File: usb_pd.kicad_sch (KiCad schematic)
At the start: 34 parts, among them J1 USB-C_GCT_USB4105-GF-A, J2 JST_SH_1x4_SM04B-SRSS-TB-LF-SN, Q1 SQS401EN-T1_BE3, U1 STUSB4500_QFN, U5 TPD4E02B04DQA, U6 TPD4E02B04DQA

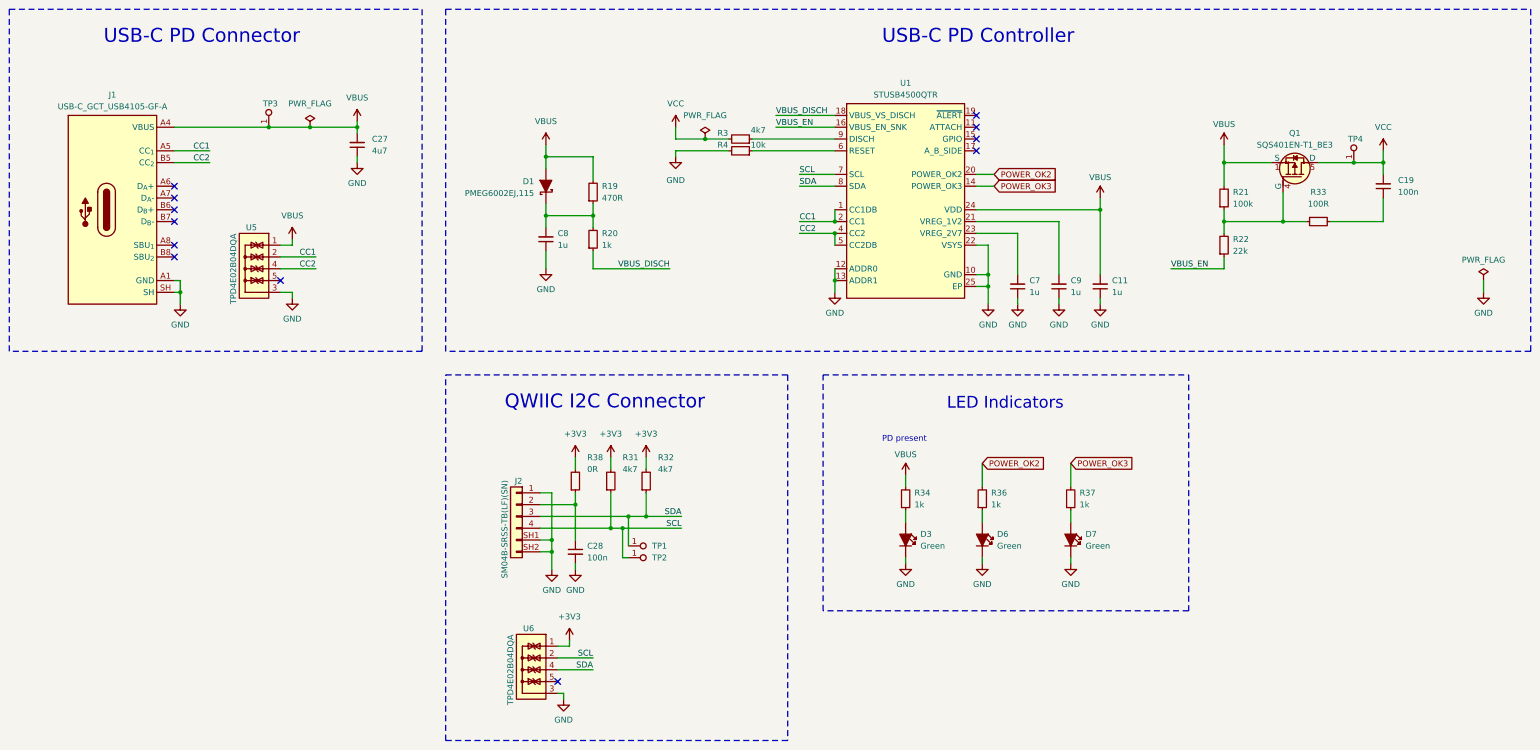
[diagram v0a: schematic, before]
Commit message: [#57006] Change capacitors to higher voltage ratings
Homogenize capacitors (to not use multiple versions of the same params)
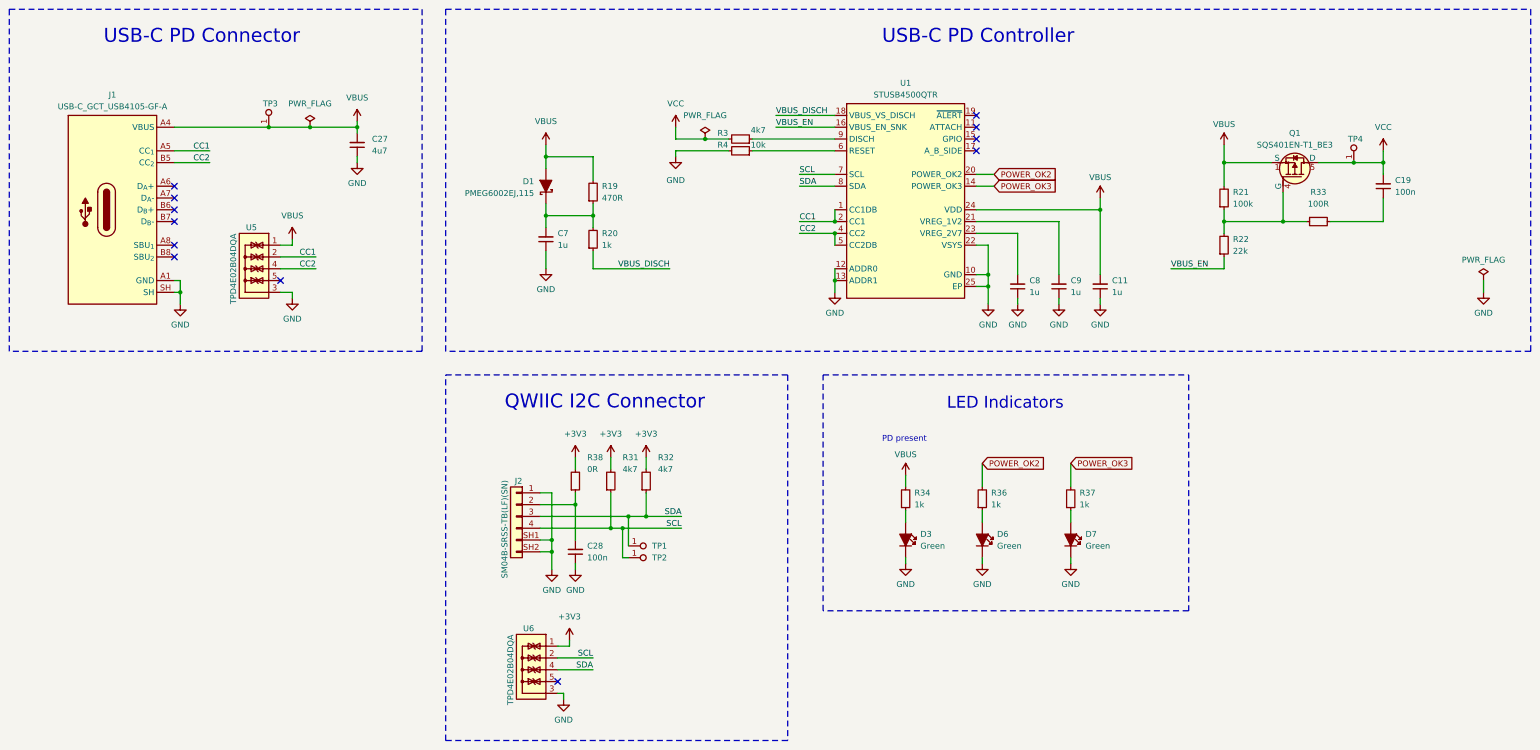
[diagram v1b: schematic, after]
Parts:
- removed C11, C7, C8, C9: C_1u_0402, antmicro-footprints:C_0402_1005Metric, symbol antmicroCapacitors0402:C_1u_0402
- removed C28: C_100n_16V_X7R_0402, antmicro-footprints:C_0402_1005Metric, symbol antmicroCapacitors0402:C_100n_16V_X7R_0402
- added C11, C7, C8, C9: C_1u_25V_0402, antmicro-footprints:C_0402_1005Metric, symbol antmicroCapacitors0402:C_1u_25V_0402
- added C28: C_100n_50V_X8L_0402, antmicro-footprints:C_0402_1005Metric, symbol antmicroCapacitors0402:C_100n_50V_X8L_0402
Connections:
- net GND: now also C11.1, C28.1, C7.1, C8.1, C9.1
- net VBUS: now also C11.2
- net at J2.2, R38.1: now also C28.2
- net at D1.K, R19.1, R20.2: now also C7.2
- net at U1.21 (VREG_1V2): now also C9.2
- net at U1.23 (VREG_2V7): now also C8.2

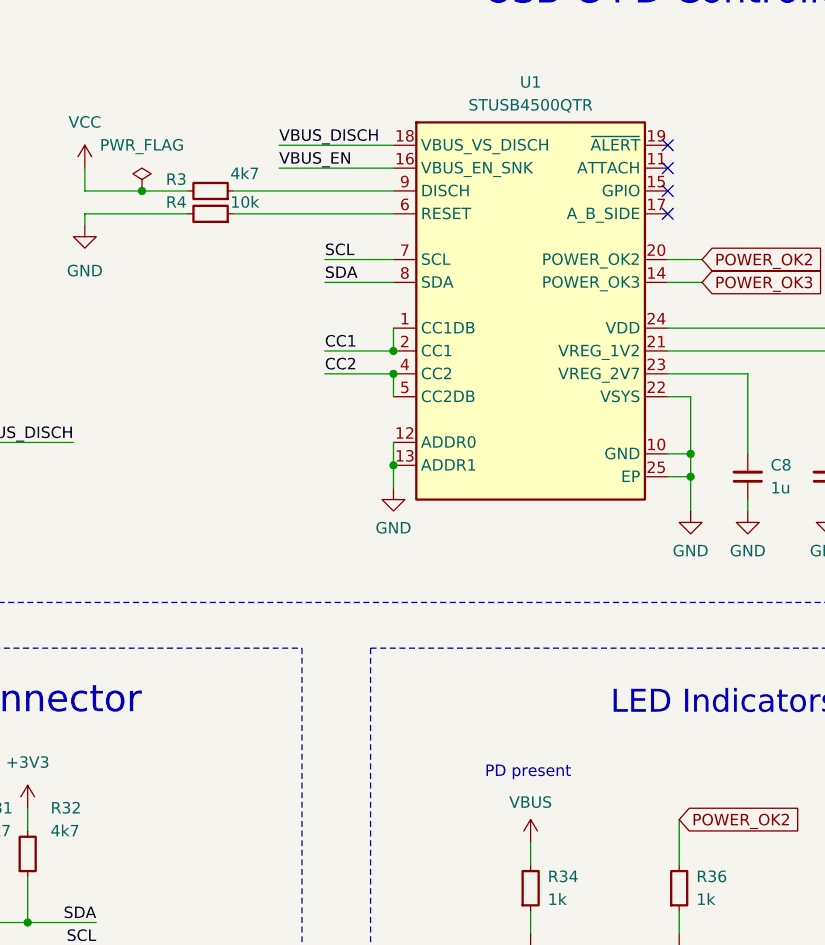
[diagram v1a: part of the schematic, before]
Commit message: [#57006] Change R3 to 0603
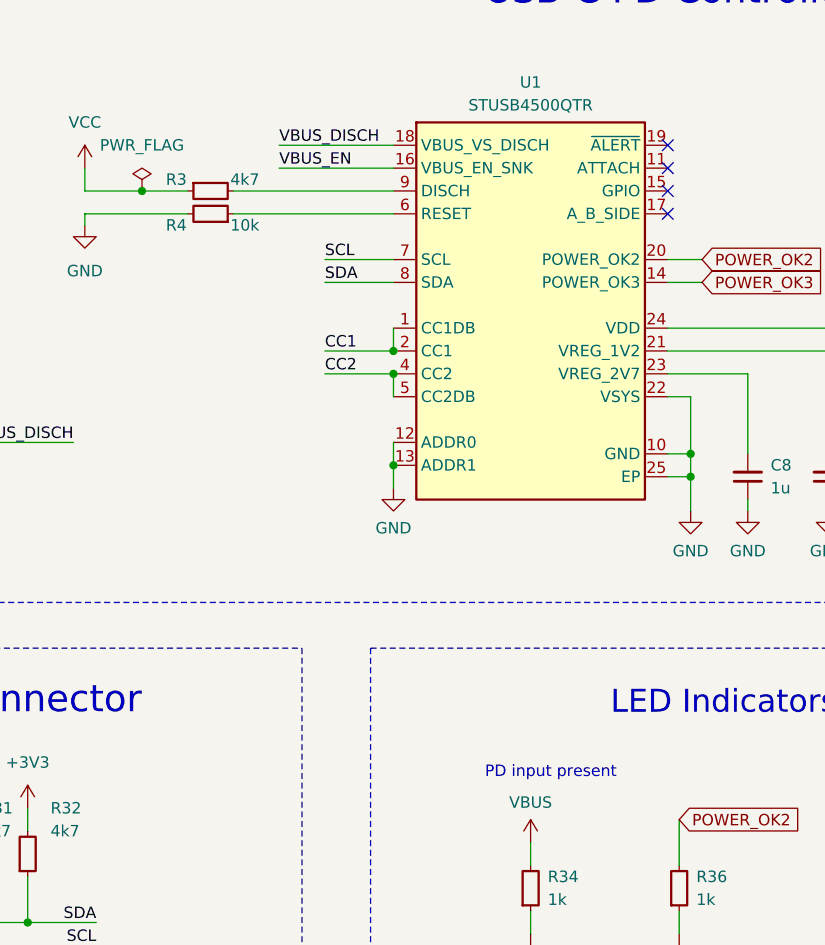
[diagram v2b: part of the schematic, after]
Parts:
- removed R3: R_4k7_0805, antmicro-footprints:R_0805_2012Metric, symbol antmicroResistorsmisc:R_4k7_0805
- added R3: R_4k7_0603, antmicro-footprints:R_0603_1608Metric, symbol antmicroResistors0603:R_4k7_0603
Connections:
- net VCC: now also R3.1
- net at U1.9 (DISCH): now also R3.2
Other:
- note added: "PD input present"
- note removed: "PD present"
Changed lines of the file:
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@@
     (comment 1 "www.antmicro.com")
   )
+  (bus_alias "I2C" (members "SDA" "SCL"))
   (junction (at 292.1 60.96) (diameter 0) (color 0 0 0 0)
   )
@@
     (effects (font (size 2.54 2.54)) (justify left bottom))
   )
-  (text "PD present\n" (at 218.44 121.285 0)
+  (text "PD input present\n" (at 218.44 121.285 0)
     (effects (font (size 1.27 1.27)) (justify left bottom))
   )
@@
     )
   )
-  (symbol (lib_id "antmicroResistorsmisc:R_4k7_0805") (at 190.5 55.88 180) (unit 1)
-    (in_bom yes) (on_board yes) (dnp no)
-    (property "Reference" "R3" (at 184.15 54.61 0)
-      (effects (font (size 1.27 1.27) (thickness 0.15)))
-    )
-    (property "Value" "R_4k7_0805" (at 170.18 43.18 0)
-      (effects (font (size 1.27 1.27) (thickness 0.15)) (justify left bottom) hide)
-    )
-    (property "Footprint" "antmicro-footprints:R_0805_2012Metric" (at 170.18 40.64 0)
-      (effects (font (size 1.27 1.27) (thickness 0.15)) (justify left bottom) hide)
-    )
-    (property "Datasheet" "https://www.bourns.com/docs/product-datasheets/cr.pdf" (at 170.18 38.1 0)
-      (effects (font (size 1.27 1.27) (thickness 0.15)) (justify left bottom) hide)
-    )
-    (property "MPN" "CR0805-FX-4701ELF" (at 170.18 35.56 0)
-      (effects (font (size 1.27 1.27) (thickness 0.15)) (justify left bottom) hide)
-    )
-    (property "Manufacturer" "Bourns" (at 170.18 33.02 0)
-      (effects (font (size 1.27 1.27) (thickness 0.15)) (justify left bottom) hide)
-    )
-    (property "License" "Apache-2.0" (at 170.18 30.48 0)
-      (effects (font (size 1.27 1.27) (thickness 0.15)) (justify left bottom) hide)
-    )
-    (property "Author" "Antmicro" (at 170.18 27.94 0)
-      (effects (font (size 1.27 1.27) (thickness 0.15)) (justify left bottom) hide)
-    )
-    (property "Val" "4k7" (at 191.77 53.975 0)
-      (effects (font (size 1.27 1.27) (thickness 0.15)))
-    )
-    (property "Tolerance" "1%" (at 170.18 45.72 0)
-      (effects (font (size 1.27 1.27)) (justify left bottom) hide)
-    )
-    (pin "1")
-    (pin "2")
-    (instances
-      (project "USB-C-power-adapter"
-        (path "/8da33aa8-79ed-467a-95ed-bf58aa0d1db6/344e016f-20ec-4e27-ac78-d9a1e9a3533b"
-          (reference "R3") (unit 1)
-        )
-      )
-    )
-  )
   (symbol (lib_id "antmicroResistors0402:R_4k7_0402") (at 160.02 132.08 90) (unit 1)
     (in_bom yes) (on_board yes) (dnp no)
@@
     )
   )
+  (symbol (lib_id "antmicroResistors0603:R_4k7_0603") (at 185.42 55.88 0) (unit 1)
+    (in_bom yes) (on_board yes) (dnp no)
+    (property "Reference" "R3" (at 184.15 54.61 0)
+      (effects (font (size 1.27 1.27) (thickness 0.15)))
+    )
+    (property "Value" "R_4k7_0603" (at 205.74 68.58 0)
+      (effects (font (size 1.27 1.27) (thickness 0.15)) (justify left bottom) hide)
+    )
+    (property "Footprint" "antmicro-footprints:R_0603_1608Metric" (at 205.74 71.12 0)
+      (effects (font (size 1.27 1.27) (thickness 0.15)) (justify left bottom) hide)
+    )
+    (property "Datasheet" "https://www.bourns.com/docs/product-datasheets/cr.pdf" (at 205.74 73.66 0)
+      (effects (font (size 1.27 1.27) (thickness 0.15)) (justify left bottom) hide)
+    )
+    (property "MPN" "CR0603-FX-4701ELF" (at 205.74 76.2 0)
+      (effects (font (size 1.27 1.27) (thickness 0.15)) (justify left bottom) hide)
+    )
+    (property "Manufacturer" "Bourns" (at 205.74 78.74 0)
+      (effects (font (size 1.27 1.27) (thickness 0.15)) (justify left bottom) hide)
+    )
+    (property "License" "Apache-2.0" (at 205.74 81.28 0)
+      (effects (font (size 1.27 1.27) (thickness 0.15)) (justify left bottom) hide)
+    )
+    (property "Author" "Antmicro" (at 205.74 83.82 0)
+      (effects (font (size 1.27 1.27) (thickness 0.15)) (justify left bottom) hide)
+    )
+    (property "Val" "4k7" (at 191.77 54.61 0)
+      (effects (font (size 1.27 1.27) (thickness 0.15)))
+    )
+    (property "Tolerance" "1%" (at 205.74 66.04 0)
+      (effects (font (size 1.27 1.27)) (justify left bottom) hide)
+    )
+    (pin "2")
+    (pin "1")
+    (instances
+      (project "USB-C-power-adapter"
+        (path "/8da33aa8-79ed-467a-95ed-bf58aa0d1db6/344e016f-20ec-4e27-ac78-d9a1e9a3533b"
+          (reference "R3") (unit 1)
+        )
+      )
+    )
+  )
   (symbol (lib_id "antmicropower:VBUS") (at 292.1 57.15 0) (unit 1)
     (in_bom yes) (on_board yes) (dnp no) (fields_autoplaced)
@@
   (symbol (lib_id "antmicroResistors0402:R_10k_0402") (at 190.5 58.42 180) (unit 1)
     (in_bom yes) (on_board yes) (dnp no)
-    (property "Reference" "R4" (at 184.15 57.15 0)
+    (property "Reference" "R4" (at 184.15 59.69 0)
       (effects (font (size 1.27 1.27) (thickness 0.15)))
     )
@@
       (effects (font (size 1.27 1.27) (thickness 0.15)) (justify left bottom) hide)
     )
-    (property "Val" "10k" (at 191.77 57.15 0)
+    (property "Val" "10k" (at 191.77 59.69 0)
       (effects (font (size 1.27 1.27) (thickness 0.15)))
     )

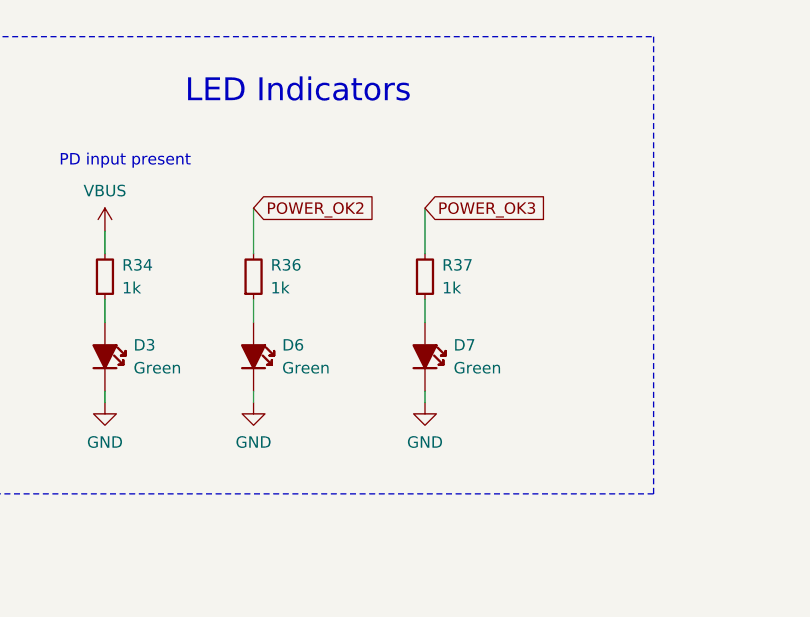
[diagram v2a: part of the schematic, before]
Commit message: [#57006] Fix POWER_OK2, POWER_OK3 LEDs
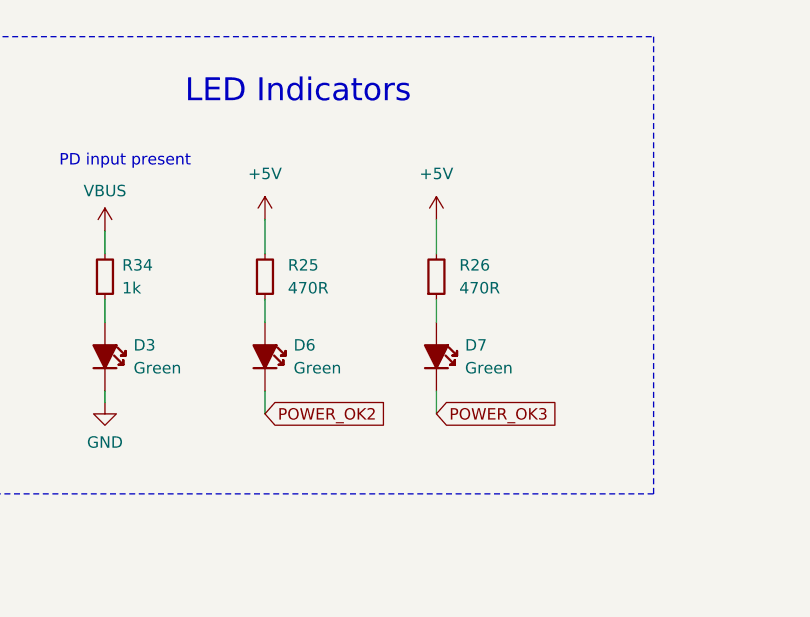
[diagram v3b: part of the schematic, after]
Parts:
- removed R36, R37: R_2k2_0402, antmicro-footprints:R_0402_1005Metric, symbol antmicroResistors0402:R_1k_0402
- added R25, R26: R_4k7_0402, antmicro-footprints:R_0402_1005Metric, symbol antmicroResistors0402:R_470R_0402
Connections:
- net GND: no longer D6.2, D7.2
- net POWER_OK2: now also D6.2
- net POWER_OK3: now also D7.2
- net at D6.1: now also R25.1
- net at D7.1: now also R26.1
- new net +5V: R25.2, R26.2
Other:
- moved on the sheet: D6, D7

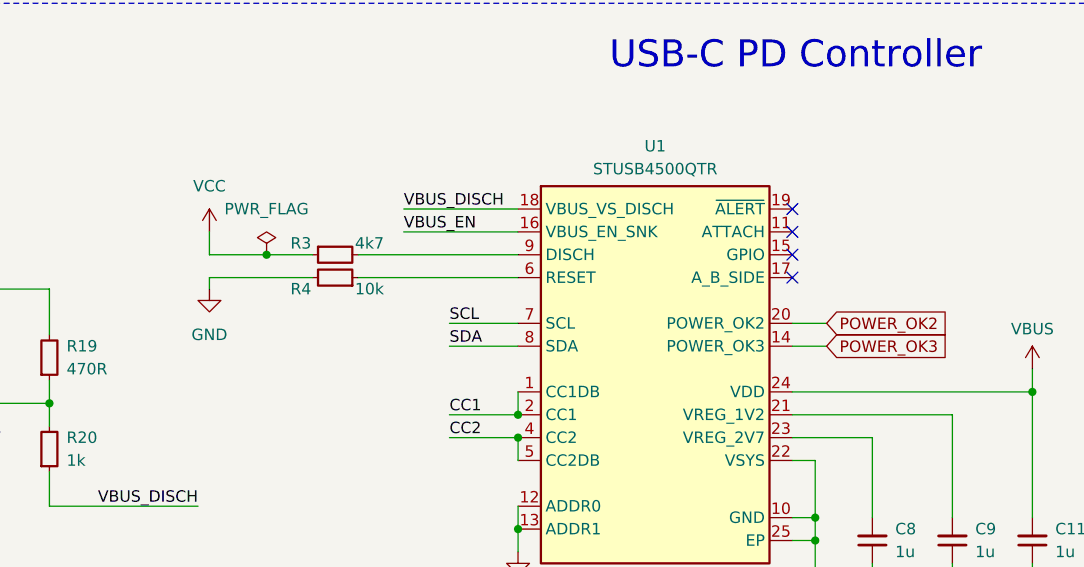
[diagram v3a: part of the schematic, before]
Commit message: [#57006] Add more testpoints
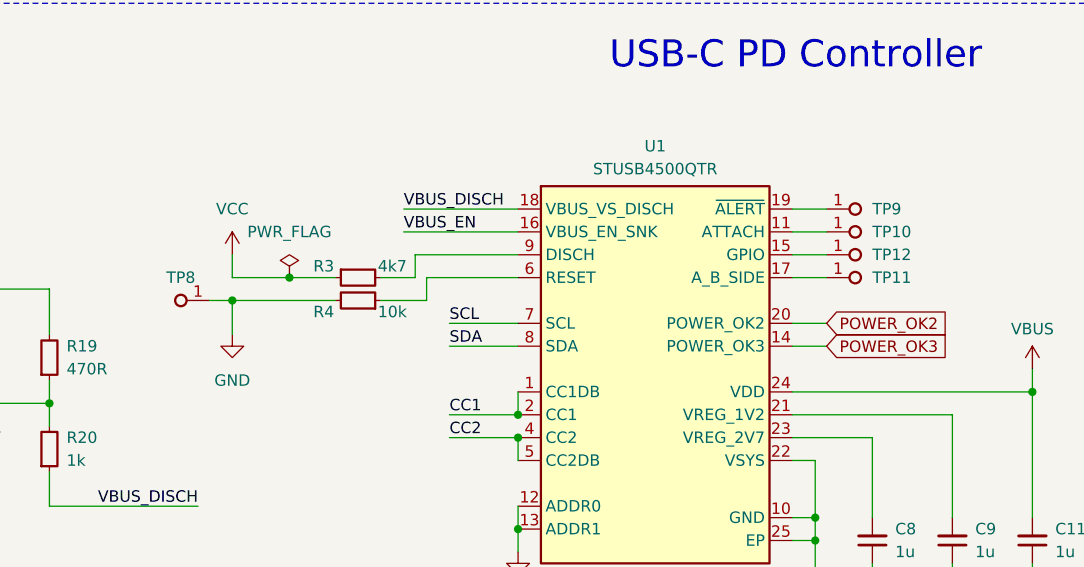
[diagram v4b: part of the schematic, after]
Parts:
- added TP10, TP11, TP12, TP8, TP9: TP_0.75mm_SMD, antmicro-footprints:TP_SMD_0.75mm, symbol antmicroTestPoints:TP_0.75mm_SMD
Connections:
- net GND: now also TP8.1
- net at U1.11 (ATTACH): now also TP10.1
- net at U1.15 (GPIO): now also TP12.1
- net at U1.17 (A_B_SIDE): now also TP11.1
- net at U1.19 (~{ALERT}): now also TP9.1
- no-connect marks 12 -> 8
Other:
- moved on the sheet: R3, R4
